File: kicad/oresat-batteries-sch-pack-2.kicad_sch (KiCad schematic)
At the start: 79 parts, among them Q24 PM45VEN, Q25 PM45VEN, Q26 PM45VEN, Q27 PM45VEN, Q30 SI7625DN-T1-GE3, Q31 SI7625DN-T1-GE3, Q32 NTR4101, Q33 NTR4101, Q34 SI7625DN-T1-GE3, Q35 SI7625DN-T1-GE3, Q36 SI7625DN-T1-GE3, Q37 SI7625DN-T1-GE3, U13 S-8209AAA-T8T1U, U14 S-8209AAA-T8T1U, U15 LTC4412, U16 LTC4412, U17 MAX17205G

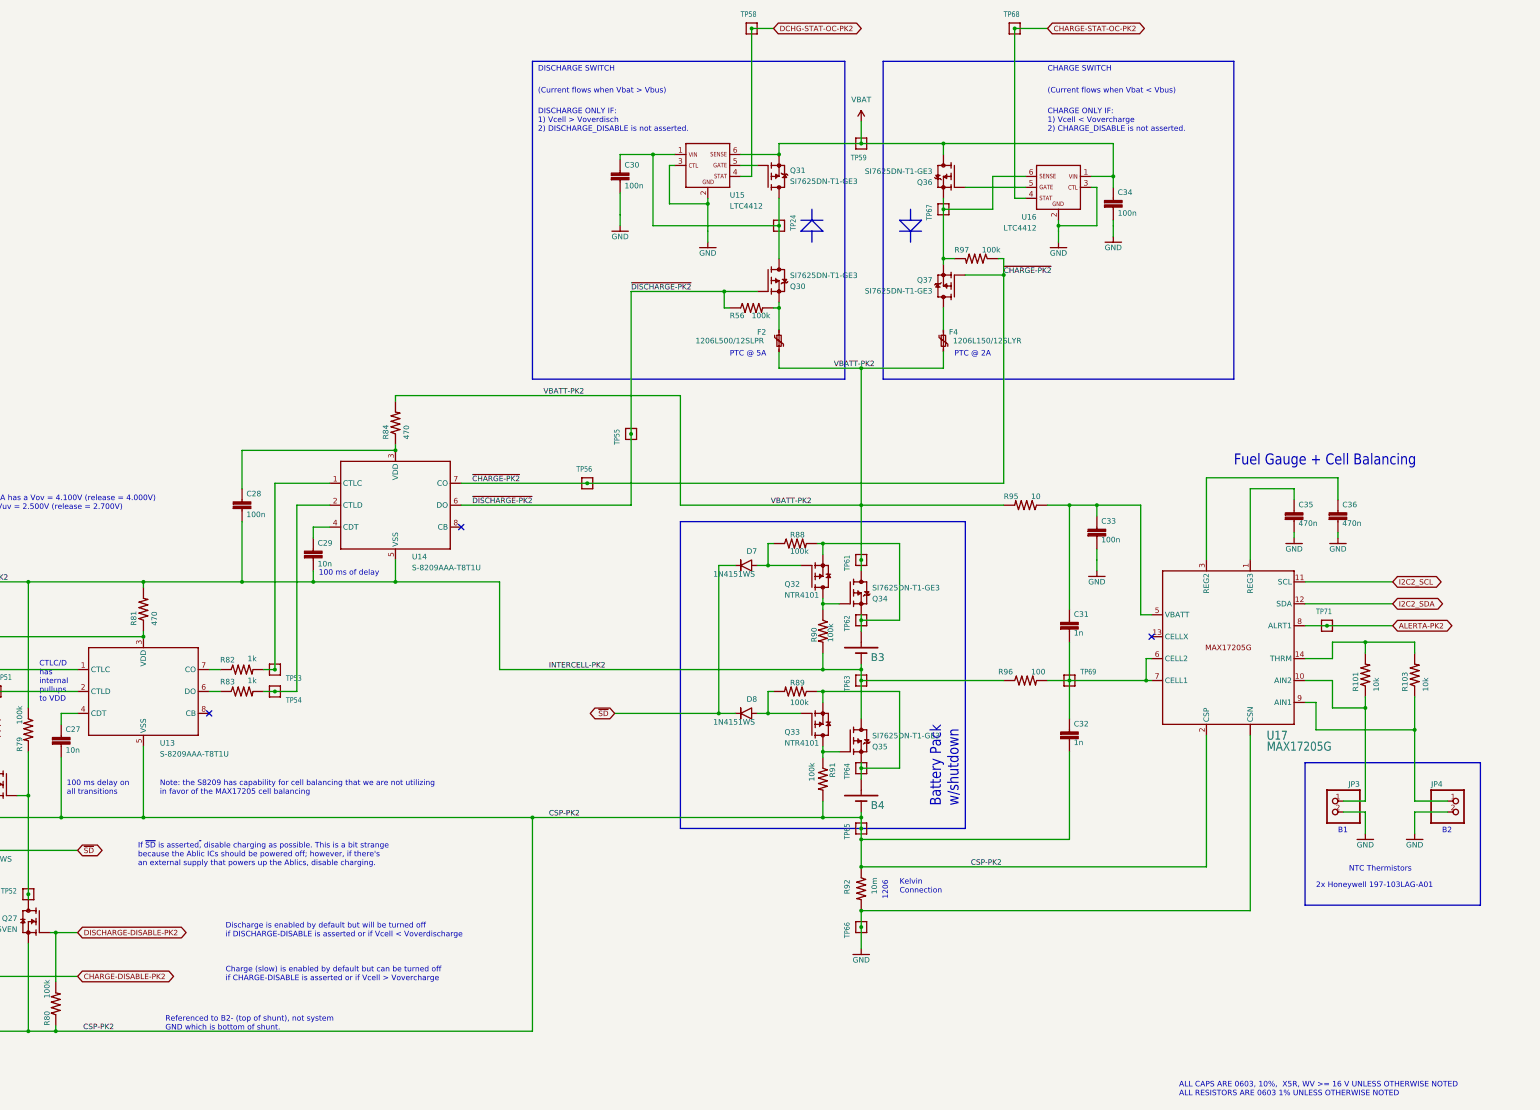
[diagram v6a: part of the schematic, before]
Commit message: Starting Battery Card 4.0
Changed root sheet to hierarchical sheet. No change to schematic or layout yet. Updated the stackup with oresat template. Switched to variables for version and date.
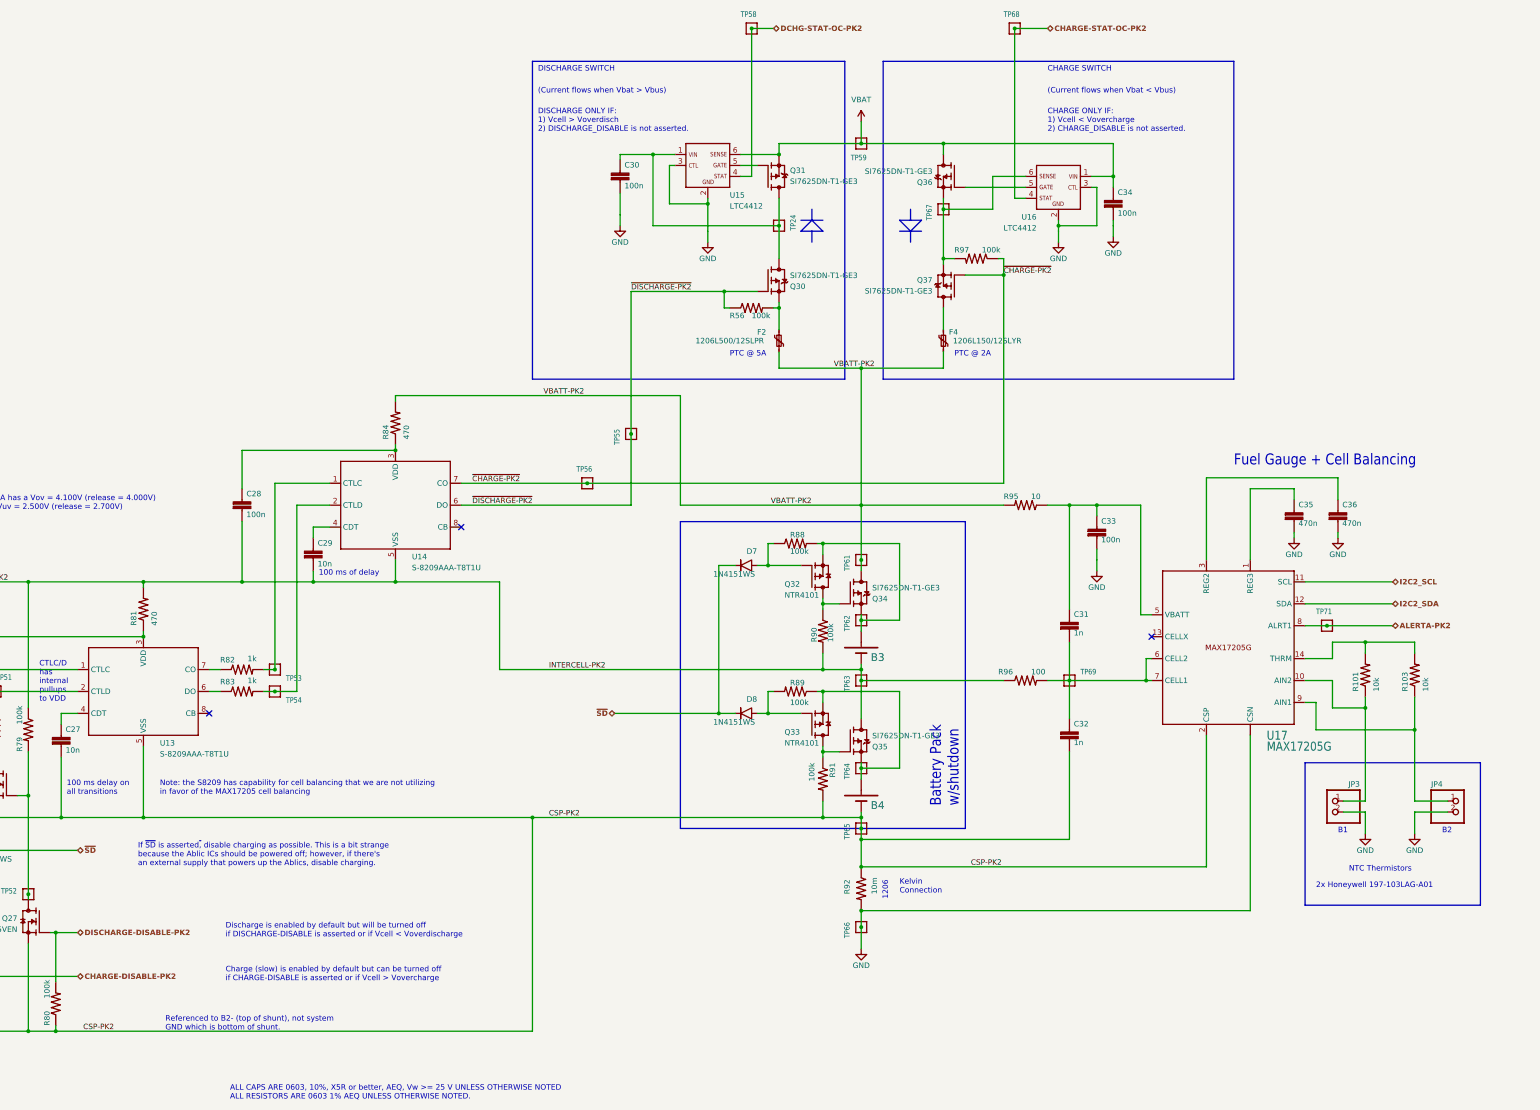
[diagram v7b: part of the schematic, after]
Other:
- note added: "ALL CAPS ARE 0603, 10%, X5R or better, AEQ, Vw >= 25 V UNLESS OTHERWISE NOTED ALL RESISTORS ARE 0603 1% AEQ UNLESS OTHERWISE NOTED."
- note removed: "ALL CAPS ARE 0603, 10%, X5R, WV >= 16 V UNLESS OTHERWISE NOTED ALL RESISTORS ARE 0603 1% UNLESS OTHERWISE NOTED"
- company: (none) -> Portland State Aerospace Society
- title: OreSat Battery Card - Pack 2 (Top) -> OreSat Battery Card

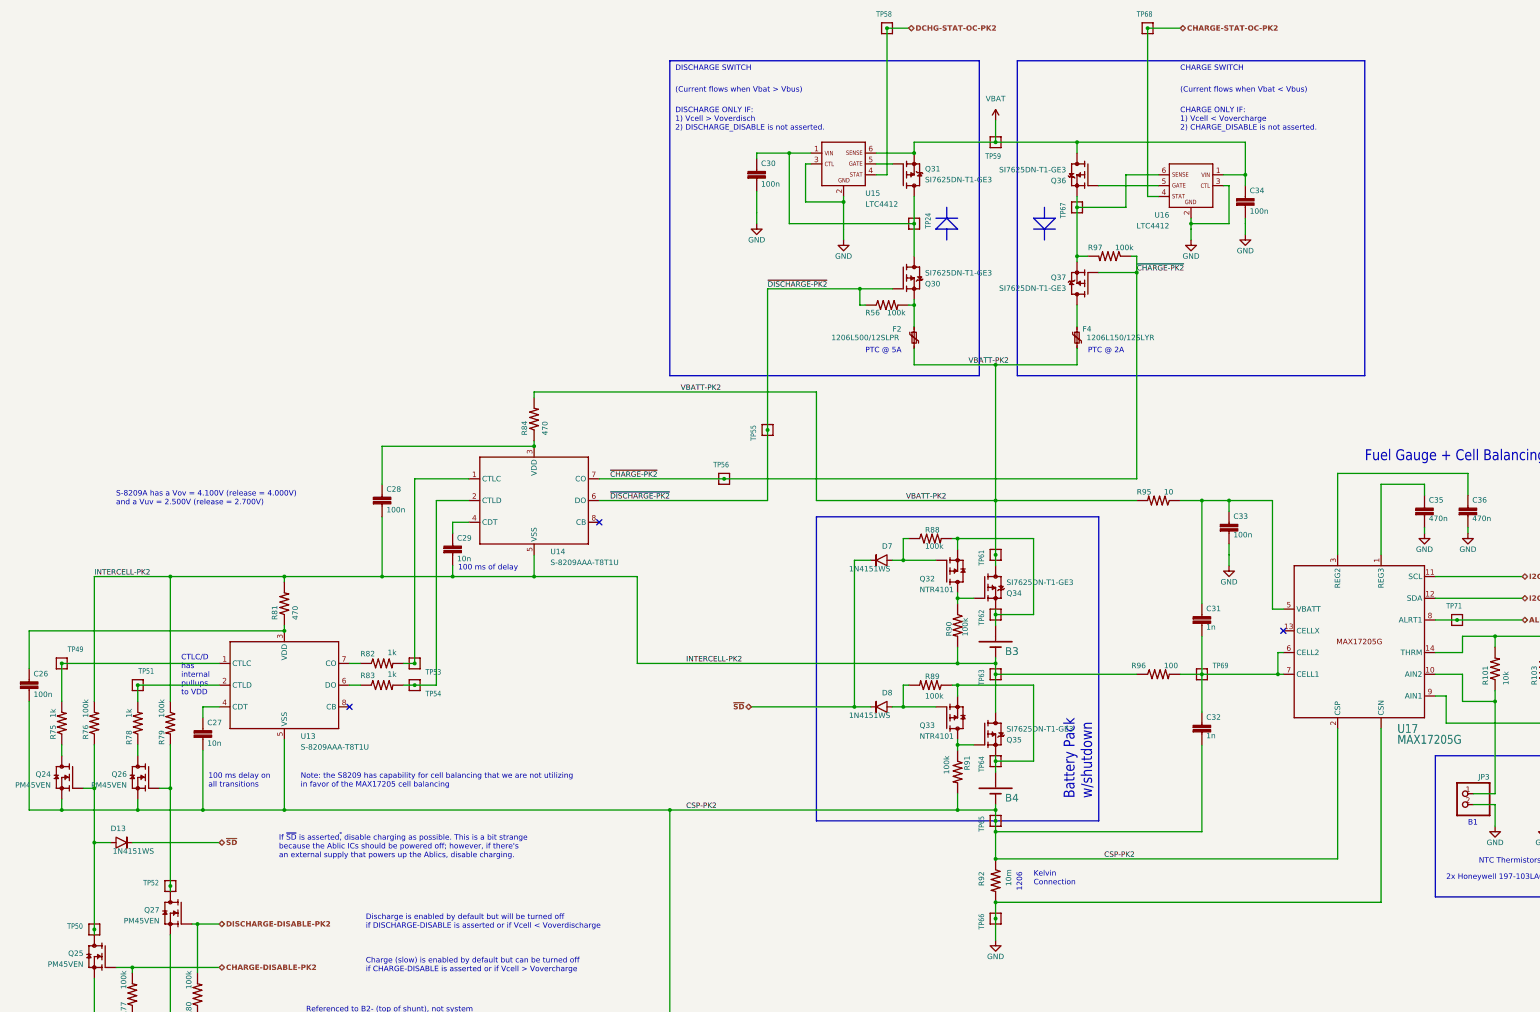
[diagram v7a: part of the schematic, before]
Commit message: Minor polishing, removing outdated OPD signals and OPD power jumper.
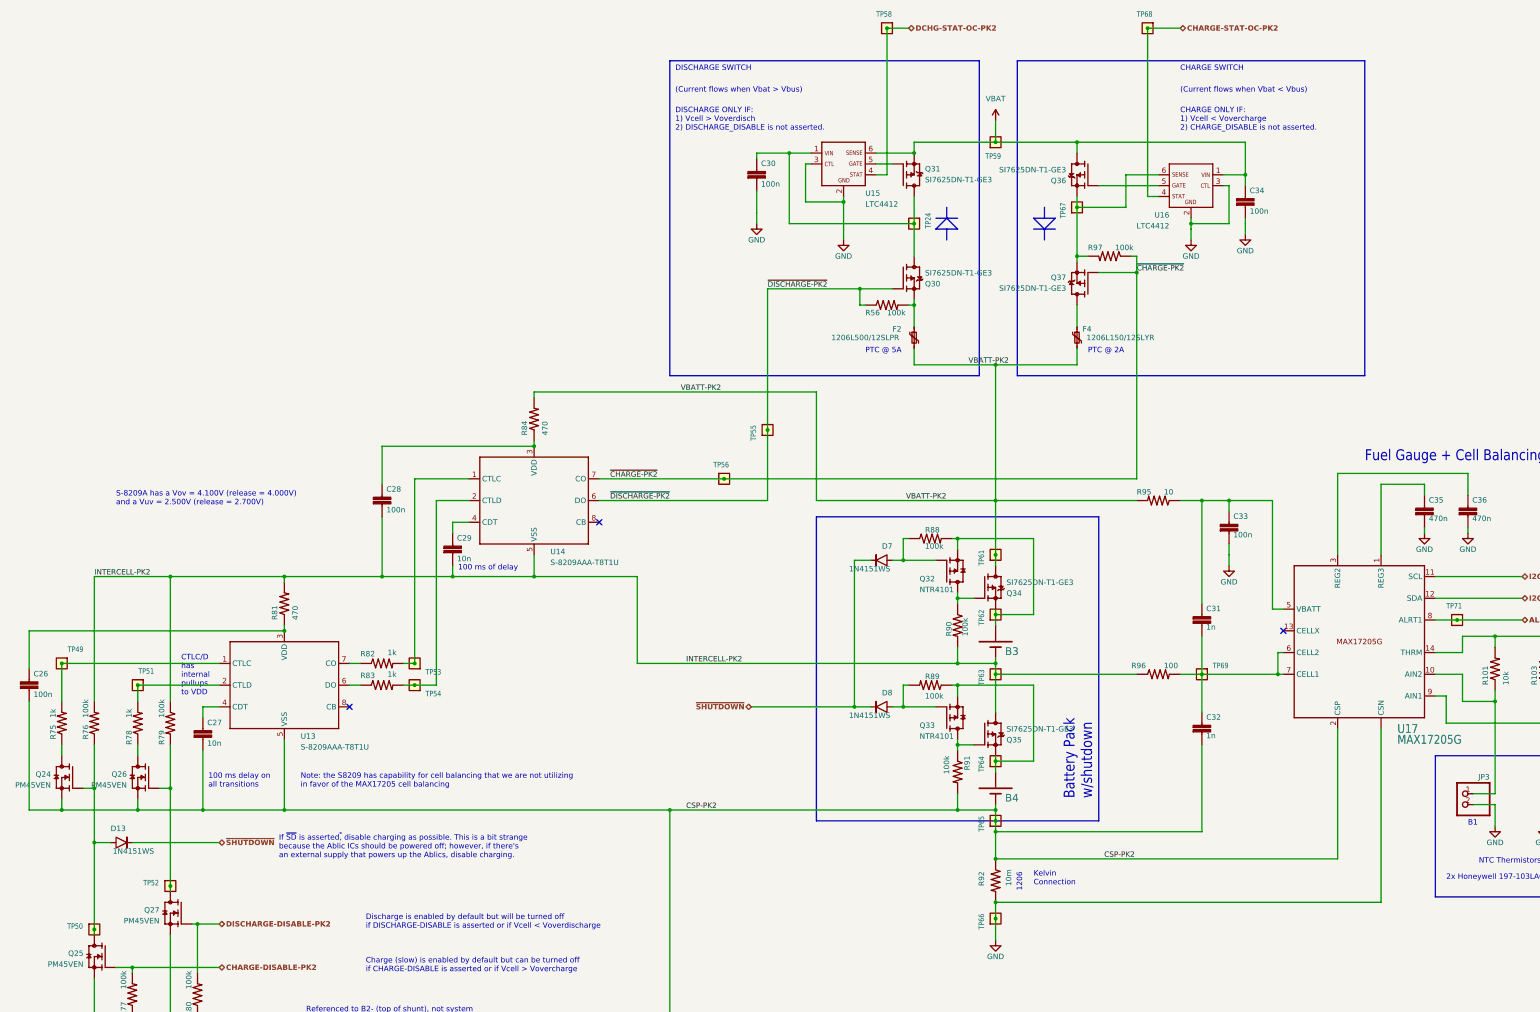
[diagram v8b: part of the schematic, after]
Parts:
- TP24, TP49, TP50, TP51, TP52, TP53, TP54, TP55, TP56, TP58, TP59, TP61, TP62, TP63, TP64, TP65, TP66, TP67, TP68, TP69, TP71: footprint oresat-batteries:1X01 -> oresat-misc:TestPoint-0.75mm-th; symbol oresat-batteries-eagle-import:TEST-POINT-LARGE-SQUARE -> oresat-misc:Test-Point-0.75mm-th; now left out of the parts list
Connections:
- net ~{SD} renamed ~{SHUTDOWN}
